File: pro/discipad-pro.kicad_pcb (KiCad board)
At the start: 2 copper layers, 76.3 x 122.8 mm, 63 parts, among them J1 AVR-ISP-6, SW0 KEYSW, SW1 KEYSW, SW10 KEYSW, SW11 KEYSW, SW12 KEYSW, SW13 KEYSW, SW14 KEYSW, SW15 KEYSW, SW16 KEYSW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

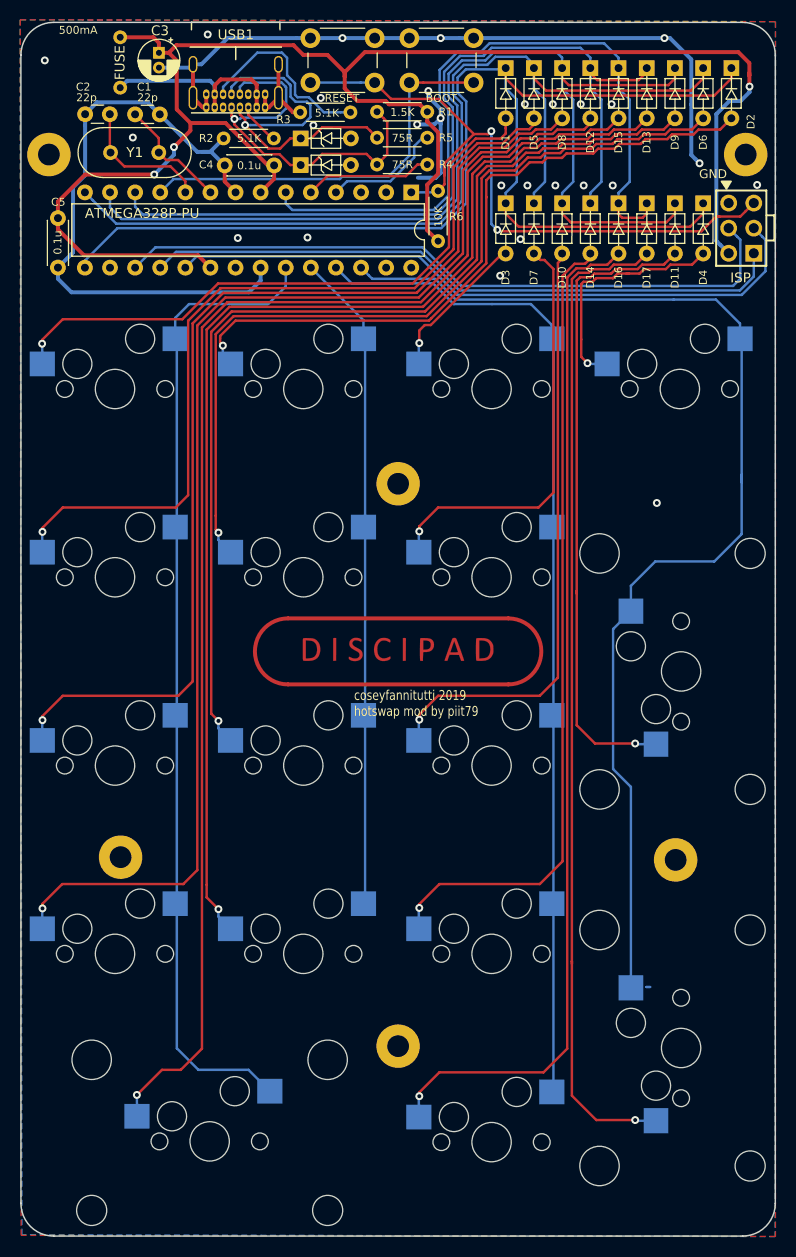
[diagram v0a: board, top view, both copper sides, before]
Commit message: Add rotary encoder support to Discipad Pro
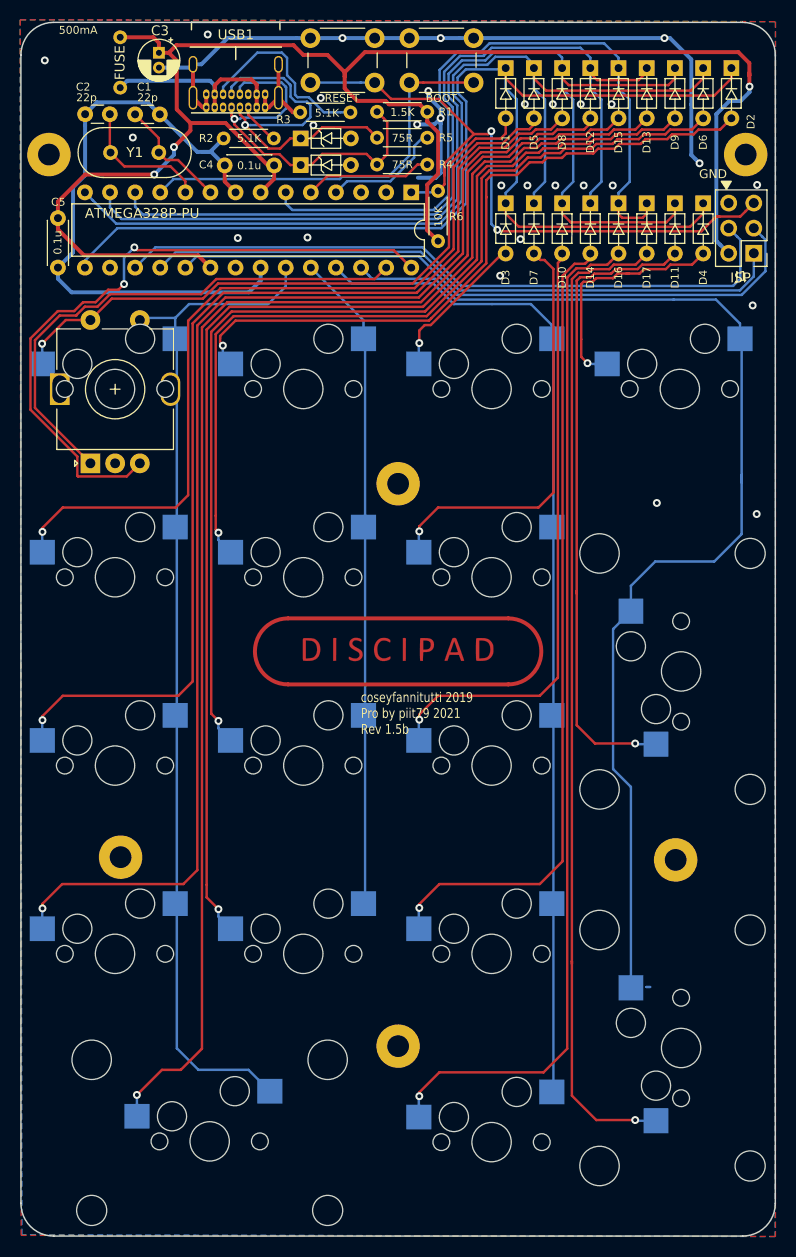
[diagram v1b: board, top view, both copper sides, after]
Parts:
- added SW17: Rotary_Encoder_Switch, discipad:RotaryEncoder_Alps_EC11E-Switch_Vertical_H20mm-for-MX, F.Cu at (112.7, 59.7)
- J1: footprint keyboard_parts:AVR_ICSP_3x2 -> Connector_PinHeader_2.54mm:PinHeader_2x03_P2.54mm_Vertical
- moved J1 2.84 mm to (179.8, 38.5), turned to 180 degrees
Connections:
- U1 pad 27: (no net) -> EN1
- U1 pad 28: (no net) -> EN2
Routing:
- net EN2: track 0.00 -> 67.5 mm, vias 0 -> 2
- net EN1: track 0.00 -> 53.4 mm
- net col0: track 101.2 -> 104.9 mm
- net GND: vias 27 -> 29
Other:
- board text added: "coseyfannitutti 2019 Pro by piit79 2021 Rev 1.5b"
- board text removed: "coseyfannitutti 2019 hotswap mod by piit79"

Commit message: Add support for splitting all 2u keys; improve ground connection
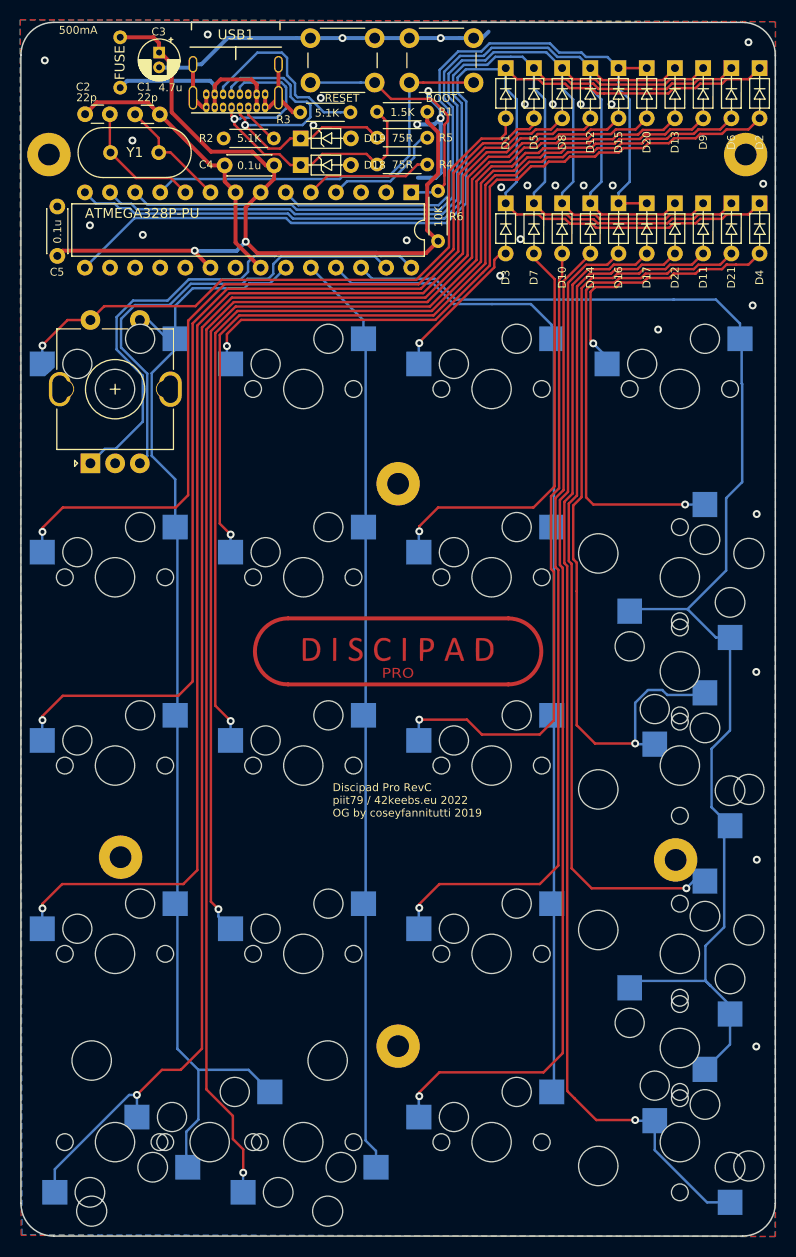
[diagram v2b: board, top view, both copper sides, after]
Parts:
- removed J1: AVR-ISP-6, Connector_PinHeader_2.54mm:PinHeader_2x03_P2.54mm_Vertical
- added D20: , discipad:D_DO-35_SOD27_P5.08mm_Horizontal, F.Cu at (169.0, 18.5)
- added D21: , discipad:D_DO-35_SOD27_P5.08mm_Horizontal, F.Cu at (177.6, 32.1)
- added D22: , discipad:D_DO-35_SOD27_P5.08mm_Horizontal, F.Cu at (171.8, 32.1)
- added SW18: KEYSW, discipad:Kailh_MX_Socket-swapped-pads, B.Cu at (134.2, 128.4)
- added SW19: KEYSW, discipad:Kailh_MX_Socket-swapped-pads, B.Cu at (172.3, 71.2)
- added SW20: KEYSW, discipad:Kailh_MX_Socket-swapped-pads, B.Cu at (172.3, 109.3)
- added SWB14: KEYSW, discipad:Kailh_MX_Socket-swapped-pads, B.Cu at (172.3, 128.4)
- added SWB15: KEYSW, discipad:Kailh_MX_Socket-swapped-pads, B.Cu at (115.2, 128.4)
- added SWB7: KEYSW, discipad:Kailh_MX_Socket-swapped-pads, B.Cu at (172.3, 90.3)
- D1, D10, D11, D12, D13, D14, D15, D16, D17, D18, D19, D2, D3, D4, D5, D6, D7, D8, D9: footprint Diode_THT:D_DO-35_SOD27_P5.08mm_Horizontal -> discipad:D_DO-35_SOD27_P5.08mm_Horizontal
- moved D4 5.71 mm to (180.4, 32.1)
- moved C5 3.82 mm to (109.4, 38.7), turned to 90 degrees
- moved D13 2.85 mm to (171.8, 18.5)
- moved D6 2.85 mm to (177.6, 18.5)
- moved D11 2.85 mm to (174.7, 32.1)
- moved D2 2.85 mm to (180.4, 18.5)
- moved D9 2.85 mm to (174.7, 18.5)
- moved SW14 0.13 mm to (172.3, 118.9)
- moved SW7 0.13 mm to (172.3, 80.8)
- moved SW15 0.07 mm to (124.8, 128.4)
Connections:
- U1 pad 16: (no net) -> unconnected-(U1-Pad16)
- U1 pad 2: (no net) -> unconnected-(U1-Pad2)
- U1 pad 21: (no net) -> unconnected-(U1-Pad21)
- U1 pad 27: EN1 -> EN2
- U1 pad 28: EN2 -> EN1
- U1 pad 3: (no net) -> unconnected-(U1-Pad3)
- USB1 pad A8: (no net) -> unconnected-(USB1-PadA8)
- USB1 pad B8: (no net) -> unconnected-(USB1-PadB8)
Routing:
- net Net-(D20-Pad2): track 0.00 -> 146.9 mm, vias 0 -> 1
- net Net-(D22-Pad2): track 0.00 -> 85.2 mm, vias 0 -> 1
- net +5V: track 174.6 -> 90.3 mm, vias 3 -> 2
- net mosi: track 69.6 -> 0.00 mm
- net GND: track 160.5 -> 93.8 mm, vias 29 -> 32
- net sck: track 66.6 -> 0.00 mm
- net miso: track 65.3 -> 0.00 mm
- net Net-(D21-Pad2): track 0.00 -> 49.5 mm, vias 0 -> 1
- net reset: track 70.2 -> 27.3 mm, vias 2 -> 0
- net col1: track 67.0 -> 94.3 mm
- net row1: track 98.0 -> 120.5 mm
- net col3: track 118.4 -> 140.4 mm
- net EN2: track 67.5 -> 46.5 mm, vias 2 -> 0
- net Net-(D15-Pad2): track 139.5 -> 152.9 mm
- net Net-(D11-Pad2): track 65.9 -> 79.3 mm
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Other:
- net class Default removed
- board text added: "Discipad Pro RevC piit79 / 42keebs.eu 2022 OG by coseyfannitutti 2019"
- board text added: "PRO"
- board text removed: "GND"
- board text removed: "ISP"
- board text removed: "coseyfannitutti 2019 Pro by piit79 2021 Rev 1.5b"

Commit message: Switch to USB-C and diode footprints from the 42. Keebs library
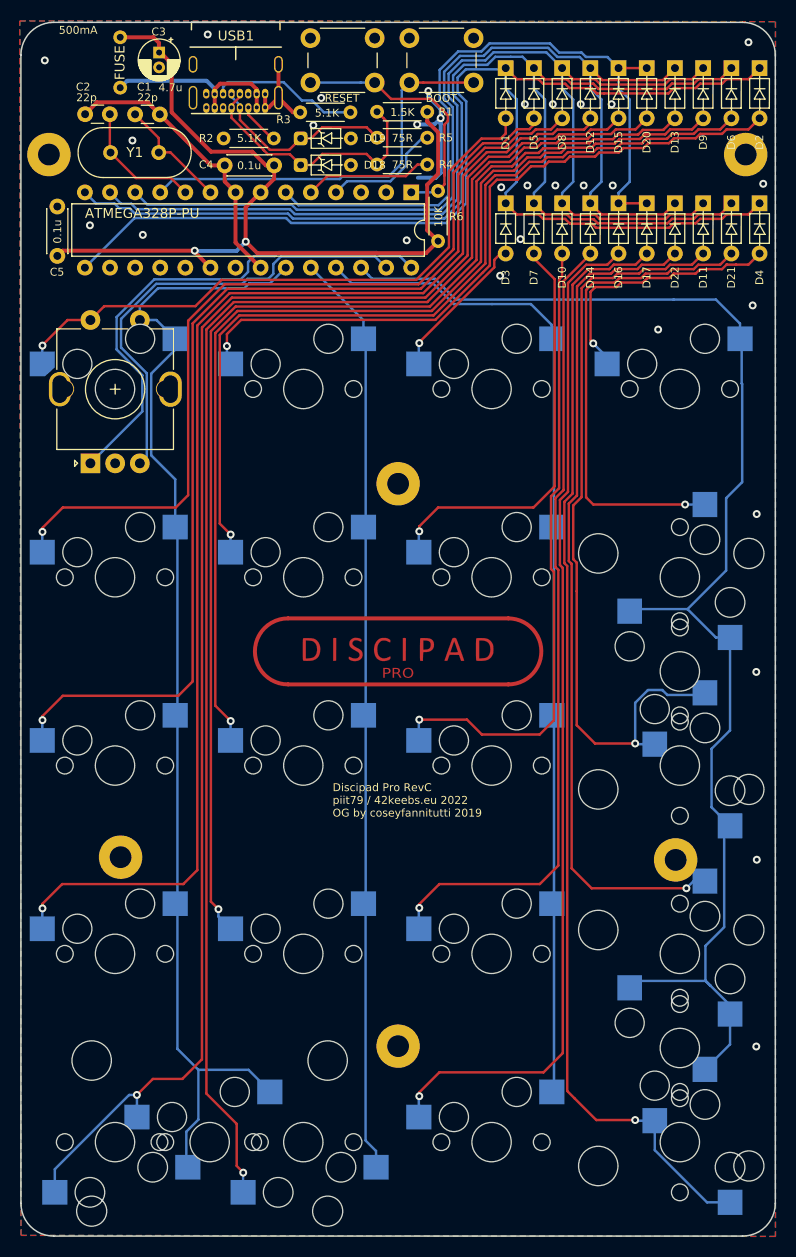
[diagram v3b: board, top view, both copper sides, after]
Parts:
- D1, D10, D11, D12, D13, D14, D15, D16, D17, D2, D20, D21, D22, D3, D4, D5, D6, D7, D8, D9: footprint discipad:D_DO-35_SOD27_P5.08mm_Horizontal -> 42keebs:D_DO-35_SOD27_P5.08mm_Horizontal
- D18, D19: footprint discipad:D_DO-35_SOD27_P5.08mm_Horizontal -> 42keebs:ZD_DO-35_SOD27_P5.08mm_Horizontal_smaller
- H1, H2, H3, H4, H5, H6: renamed from REF**; value MountingHole_2.2mm_M2_Pad -> MountingHole
- USB1: footprint Type-C:USB_C_GCT_USB4085 -> 42keebs:USB_C_GCT_USB4085-offset-pads
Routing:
- net GND: track 93.8 -> 52.5 mm, vias 32 -> 30
- net Net-(D19-Pad1): track 36.8 -> 19.5 mm, vias 1 -> 0
- net Net-(D18-Pad1): track 38.7 -> 26.5 mm, vias 1 -> 0
- net Net-(R3-Pad2): track 19.3 -> 15.1 mm
- net col0: track 116.3 -> 118.0 mm
- net VCC: track 20.2 -> 19.1 mm
- net EN1: track 52.5 -> 51.8 mm
- net Net-(D15-Pad2): track 152.9 -> 153.6 mm
